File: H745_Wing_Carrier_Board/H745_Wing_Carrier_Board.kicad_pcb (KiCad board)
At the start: 2 copper layers, 12 parts, among them J1 Conn_01x09, J10 SM03B-GHS-TB(LF)(SN)-, J11 SM03B-GHS-TB(LF)(SN)-, J12 SM06B-GHS-TB(LF)(SN), J2 Conn_01x03, J3 Conn_01x14, J4 Conn_01x14, J5 Conn_01x09, J6 Conn_01x14, J7 Conn_01x09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

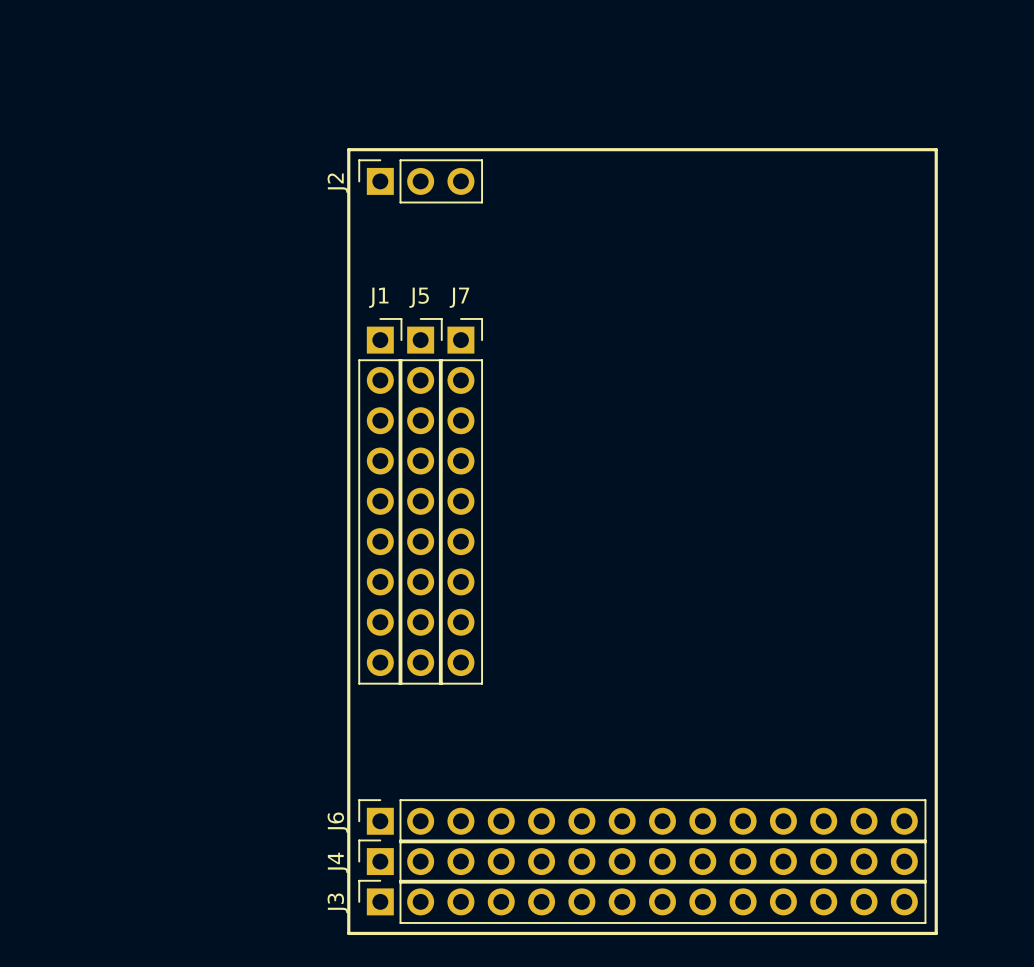
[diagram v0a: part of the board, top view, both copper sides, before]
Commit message: Added footprints for ux
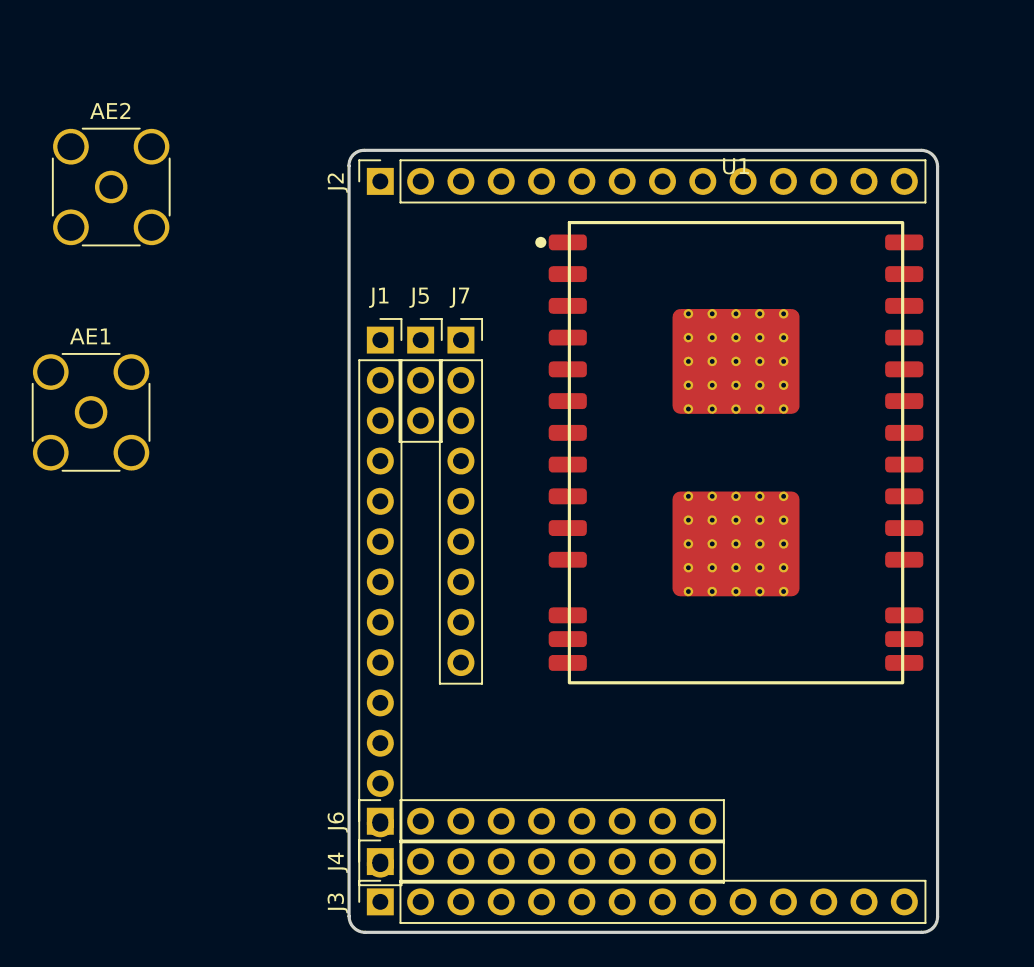
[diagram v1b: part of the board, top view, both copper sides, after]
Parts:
- added AE1: Antenna_Shield, Connector_Coaxial:SMA_Amphenol_132134-16_Vertical, F.Cu at (91.4, 142.2)
- added AE2: Antenna_Shield, Connector_Coaxial:SMA_Amphenol_132134-16_Vertical, F.Cu at (92.7, 128.0)
- added U1: RFD900ux, Footprints:RFD900ux, F.Cu at (132.1, 144.8)
- J1: value Conn_01x09 -> Conn_01x14; footprint Connector_PinSocket_2.54mm:PinSocket_1x09_P2.54mm_Vertical -> Connector_PinSocket_2.54mm:PinSocket_1x14_P2.54mm_Vertical
- J2: value Conn_01x03 -> Conn_01x14; footprint Connector_PinSocket_2.54mm:PinSocket_1x03_P2.54mm_Vertical -> Connector_PinSocket_2.54mm:PinSocket_1x14_P2.54mm_Vertical
- J4, J6: value Conn_01x14 -> Conn_01x09; footprint Connector_PinSocket_2.54mm:PinSocket_1x14_P2.54mm_Vertical -> Connector_PinSocket_2.54mm:PinSocket_1x09_P2.54mm_Vertical
- J5: value Conn_01x09 -> Conn_01x03; footprint Connector_PinSocket_2.54mm:PinSocket_1x09_P2.54mm_Vertical -> Connector_PinSocket_2.54mm:PinSocket_1x03_P2.54mm_Vertical
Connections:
- net /Audio_Out renamed /Connector_Breakouts/Audio_Out
- net /LED renamed /Peripheral_Breakouts/S11
- net /Rx4 renamed /Peripheral_Breakouts/Rts7
- net /Rx8 renamed /Peripheral_Breakouts/Rx1
- net /S1 renamed /Peripheral_Breakouts/S12
- net /S10 renamed /Servo_Outputs/S10
- net /S2 renamed /Servo_Outputs/S2
- net /S3 renamed /Servo_Outputs/S3
- net /S4 renamed /Servo_Outputs/S4
- net /S5 renamed /Servo_Outputs/S5
- net /S6 renamed /Servo_Outputs/S6
- net /S7 renamed /Servo_Outputs/S7
- net /S8 renamed /Servo_Outputs/S8
- net /S9 renamed /Servo_Outputs/S9
- net /Tx6 renamed /Peripheral_Breakouts/Tx7
- net /Tx8 renamed /Peripheral_Breakouts/Tx1
- J1 pad 2: GND -> +5V
- J1 pad 3: GND -> /Peripheral_Breakouts/LED
- J1 pad 4: GND -> /Peripheral_Breakouts/VTx
- J1 pad 5: GND -> +9V
- J1 pad 7: GND -> /Peripheral_Breakouts/Tx8
- J1 pad 8: GND -> /Peripheral_Breakouts/Rx8
- J1 pad 9: GND -> /Peripheral_Breakouts/Tx4
- J10 pad 3: /C1 -> /Connector_Breakouts/C1
- J11 pad 3: /C2 -> /Connector_Breakouts/C2
- J12 pad 4: /VTx -> /Connector_Breakouts/VTx
- J2 pad 2: /Vx -> /Peripheral_Breakouts/Vx
- J3 pad 12: /Rx6 -> /Peripheral_Breakouts/Rx7
- J3 pad 13: /4v5 -> +5V
- J3 pad 2: +5V -> /Peripheral_Breakouts/Vx
- J3 pad 4: /VTx -> /Peripheral_Breakouts/C2
- J3 pad 5: +9V -> /Peripheral_Breakouts/Vsw
- J3 pad 9: /Tx4 -> /Peripheral_Breakouts/Cts7
- J4 pad 2: /Vx -> GND
- J4 pad 3: /S12 -> GND
- J4 pad 4: /C1 -> GND
- J4 pad 5: +9V -> GND
- J4 pad 7: /Tx3 -> GND
- J4 pad 8: /Rx3 -> GND
- J4 pad 9: /DA1 -> GND
- J5 pad 1: /Vx -> GND
- J5 pad 2: /Vx -> /Servo_Outputs/Vx
- J5 pad 3: /Vx -> /Servo_Outputs/S1
- J6 pad 1: GND -> /Servo_Outputs/Vx
- J6 pad 2: /Vx -> /Servo_Outputs/Vx
- J6 pad 3: /S11 -> /Servo_Outputs/Vx
- J6 pad 4: /C2 -> /Servo_Outputs/Vx
- J6 pad 5: /Vsw -> /Servo_Outputs/Vx
- J6 pad 6: GND -> /Servo_Outputs/Vx
- J6 pad 7: /Tx1 -> /Servo_Outputs/Vx
- J6 pad 8: /Rx1 -> /Servo_Outputs/Vx
- J6 pad 9: /Cts7 -> /Servo_Outputs/Vx
- J8 pad 2: /Tx7 -> /Connector_Breakouts/Tx7
- J8 pad 3: /Rx7 -> /Connector_Breakouts/Rx7
- J8 pad 4: /Rts7 -> /Connector_Breakouts/Rts7
- J8 pad 5: /Cts7 -> /Connector_Breakouts/Cts7
- J9 pad 2: /4v5 -> /Connector_Breakouts/4v5
- J9 pad 3: /Rx6 -> /Connector_Breakouts/Rx6
- J9 pad 4: /Tx4 -> /Connector_Breakouts/Tx4
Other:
- board outline added: 37.1 x 49.3 mm

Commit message: Fixed layout
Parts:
- added ?: , , B.Cu at (154.5, 137.6)
- added ?: , , B.Cu at (154.0, 147.2)
- added G***: LOGO, LOGO, F.Cu at (130.7, 160.8)
- added J13: USB_B_Micro, Connector_USB:USB_Micro-B_Molex-105017-0001, F.Cu at (127.8, 127.9)
- added JP1: UART_Switch, Footprints:UART_Switch, F.Cu at (161.5, 115.0)
- added JP2: UART_Switch, Footprints:UART_Switch, F.Cu at (161.5, 118.0)
- added U2: USBLC6-2SC6, Package_TO_SOT_SMD:SOT-23-6, F.Cu at (137.0, 128.1)
- J1, J2, J3, J4, J5, J6, J7, U1: moved to B.Cu
- moved AE1 51.1 mm to (138.8, 161.4)
- moved AE2 44.9 mm to (122.8, 161.4)
- moved J2 42.5 mm to (109.2, 170.2), turned to -90 degrees
- moved J8 37.9 mm to (165.1, 102.1), turned to 90 degrees
- moved J1 35.0 mm to (109.2, 172.7), turned to -90 degrees
- moved J4 33.3 mm to (109.2, 137.2), turned to 180 degrees
- moved J6 30.9 mm to (111.8, 137.2), turned to 180 degrees
- moved J5 11.1 mm to (109.2, 127.0), turned to -90 degrees
- moved J3 5.46 mm to (109.2, 167.6), turned to -90 degrees
- moved U1 2.72 mm to (131.9, 142.1), turned to 180 degrees
- moved J7 0.65 mm to (114.3, 137.2), turned to 180 degrees
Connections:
- net Net-(AE1-Pad1) renamed /RFD900ux/ANT2
- net Net-(AE2-Pad1) renamed /RFD900ux/ANT1
- U1 pad 2: /RFD900ux/USB_DM -> /RFD900ux/USB_D-
- U1 pad 3: /RFD900ux/USB_DP -> /RFD900ux/USB_D+
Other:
- copper layers 2 -> 4
- board text added: "JLCJLCJLC"

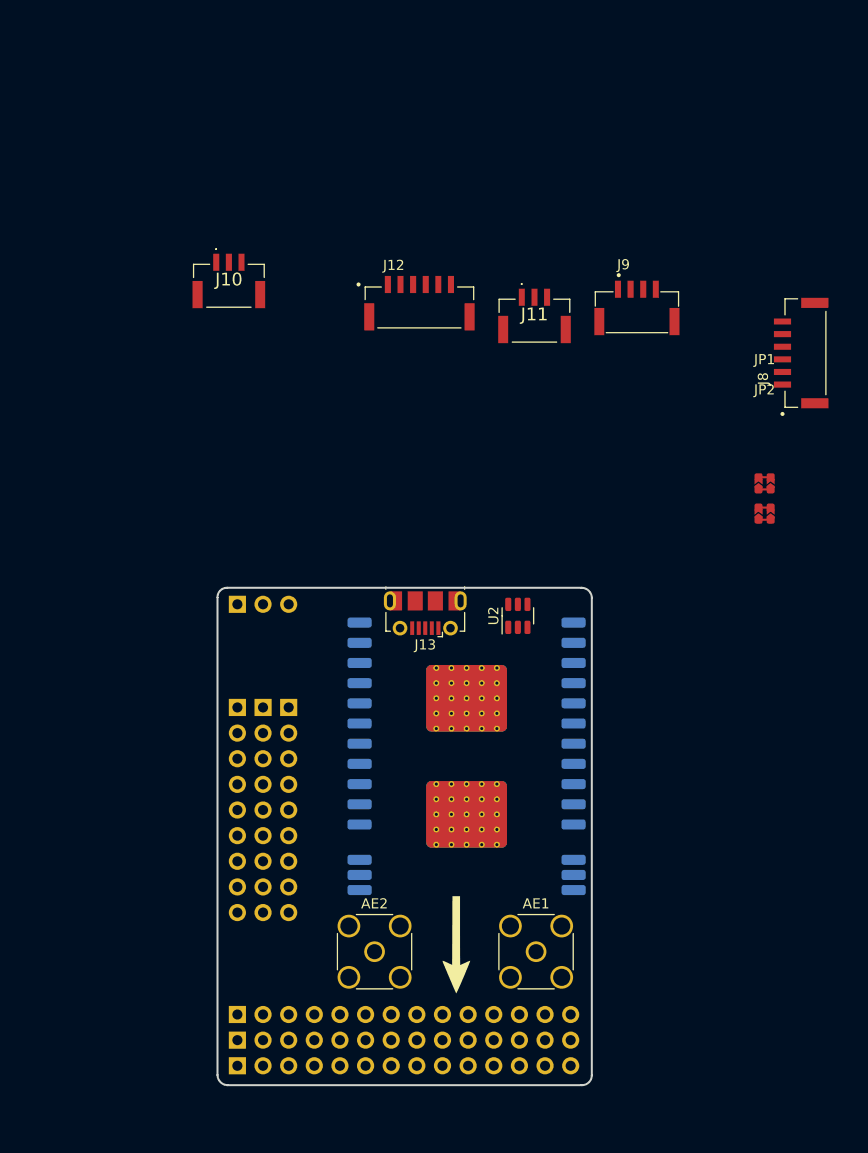
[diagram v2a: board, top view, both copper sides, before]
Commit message: Traced together some stuff:
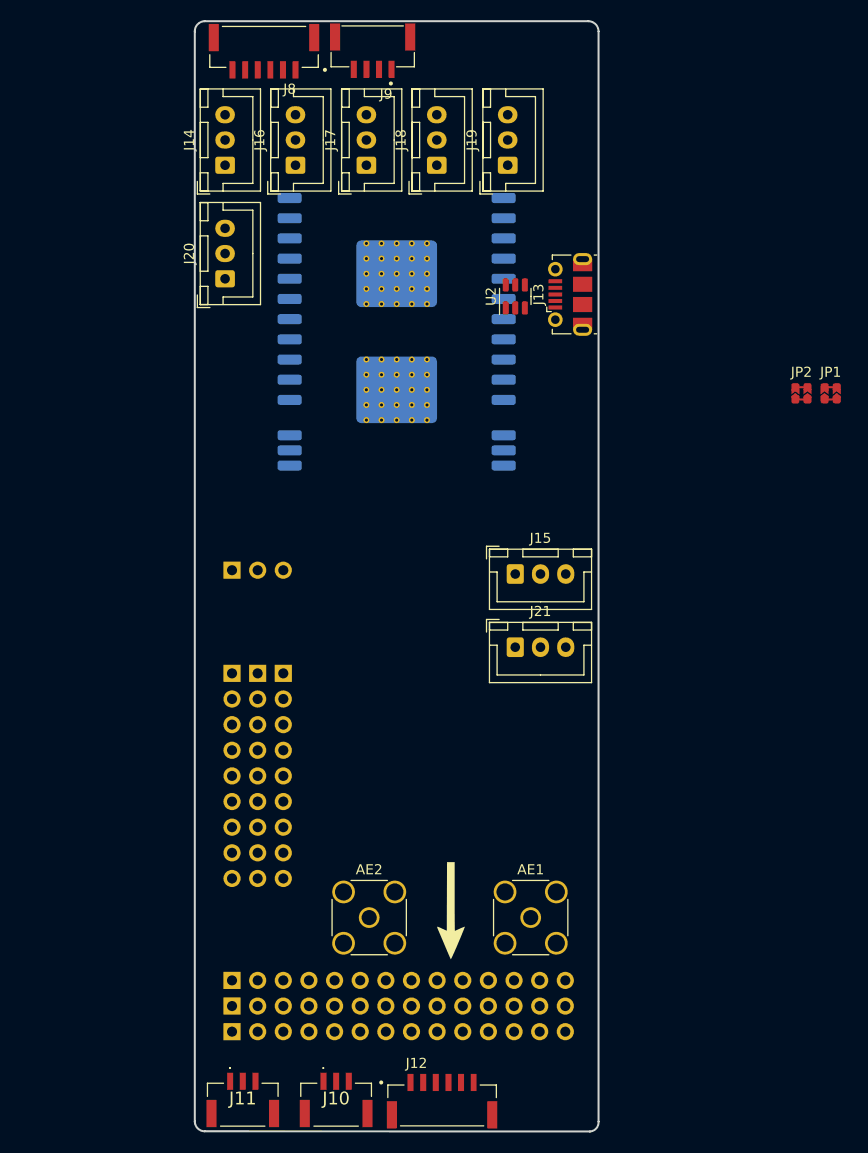
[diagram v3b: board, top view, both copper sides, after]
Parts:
- removed ? (x2): , 
- added J14: JST 3 Pin, Connector_JST:JST_XH_B3B-XH-A_1x03_P2.50mm_Vertical, F.Cu at (108.0, 83.5)
- added J15: JST 3 Pin, Connector_JST:JST_XH_B3B-XH-A_1x03_P2.50mm_Vertical, F.Cu at (136.8, 124.0)
- added J16: JST 3 Pin, Connector_JST:JST_XH_B3B-XH-A_1x03_P2.50mm_Vertical, F.Cu at (115.0, 83.5)
- added J17: JST 3 Pin, Connector_JST:JST_XH_B3B-XH-A_1x03_P2.50mm_Vertical, F.Cu at (122.0, 83.5)
- added J18: JST 3 Pin, Connector_JST:JST_XH_B3B-XH-A_1x03_P2.50mm_Vertical, F.Cu at (129.0, 83.5)
- added J19: JST 3 Pin, Connector_JST:JST_XH_B3B-XH-A_1x03_P2.50mm_Vertical, F.Cu at (136.0, 83.5)
- added J20: JST 3 Pin, Connector_JST:JST_XH_B3B-XH-A_1x03_P2.50mm_Vertical, F.Cu at (108.0, 94.8)
- added J21: JST 3 Pin, Connector_JST:JST_XH_B3B-XH-A_1x03_P2.50mm_Vertical, F.Cu at (136.8, 131.2)
- moved J11 82.9 mm to (109.8, 175.1)
- moved J10 81.8 mm to (119.0, 175.1)
- moved J12 79.1 mm to (129.5, 176.2)
- moved J8 61.1 mm to (111.9, 72.2), turned to 180 degrees
- moved U1 42.6 mm to (125.0, 100.0)
- moved J9 37.1 mm to (122.6, 71.7), turned to 180 degrees
- moved J13 34.7 mm to (142.2, 96.3), turned to 90 degrees
- moved U2 31.6 mm to (136.8, 96.5)
- moved JP2 12.5 mm to (165.1, 106.1)
- moved JP1 11.1 mm to (168.0, 106.1)
- moved AE1 3.42 mm to (138.3, 158.0)
- moved AE2 3.42 mm to (122.3, 158.0)
- moved J2 3.42 mm to (108.7, 166.8)
- moved G*** 3.42 mm to (130.2, 157.4)
- moved J5 3.42 mm to (108.7, 123.6)
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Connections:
- net /Connector_Breakouts/Audio_Out renamed /Audio_Out
- net /Servo_Outputs/Vx renamed /Connector_Breakouts/Servo_PWR
- J1 pad 3: /Peripheral_Breakouts/LED -> /LED
- J1 pad 4: /Peripheral_Breakouts/VTx -> /VTX_Out
- J10 pad 3: /Connector_Breakouts/C1 -> /Camera1
- J11 pad 1: +9V -> /Vsw
- J11 pad 3: /Connector_Breakouts/C2 -> /Camera2
- J12 pad 4: /Connector_Breakouts/VTx -> /VTX_Out
- J2 pad 4: /Peripheral_Breakouts/C1 -> /Camera1
- J3 pad 10: /Peripheral_Breakouts/Rts7 -> /Rts7
- J3 pad 11: /Peripheral_Breakouts/Tx7 -> /Tx7
- J3 pad 12: /Peripheral_Breakouts/Rx7 -> /Rx7
- J3 pad 4: /Peripheral_Breakouts/C2 -> /Camera2
- J3 pad 5: /Peripheral_Breakouts/Vsw -> /Vsw
- J3 pad 7: /Peripheral_Breakouts/Tx1 -> /Tx1
- J3 pad 8: /Peripheral_Breakouts/Rx1 -> /Rx1
- J3 pad 9: /Peripheral_Breakouts/Cts7 -> /Cts7
- J5 pad 3: /Servo_Outputs/S1 -> /Connector_Breakouts/Servo1_PWM
- J7 pad 1: /Servo_Outputs/S2 -> /Connector_Breakouts/Servo2_PWM
- J7 pad 2: /Servo_Outputs/S3 -> /Connector_Breakouts/Servo3_PWM
- J7 pad 3: /Servo_Outputs/S4 -> /Connector_Breakouts/Servo4_PWM
- J7 pad 4: /Servo_Outputs/S5 -> /Connector_Breakouts/Servo5_PWM
- J7 pad 5: /Servo_Outputs/S6 -> /Connector_Breakouts/Servo6_PWM
- J8 pad 2: /Connector_Breakouts/Tx7 -> /Tx7
- J8 pad 3: /Connector_Breakouts/Rx7 -> /Rx7
- J8 pad 4: /Connector_Breakouts/Rts7 -> /Rts7
- J8 pad 5: /Connector_Breakouts/Cts7 -> /Cts7
- JP2 pad 2: unconnected-(JP2-TX1-Pad2) -> /Tx1
- JP2 pad 4: unconnected-(JP2-RX2-Pad4) -> /Rx1
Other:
- board size 37.1 x 49.3 mm -> 40 x 110 mm
